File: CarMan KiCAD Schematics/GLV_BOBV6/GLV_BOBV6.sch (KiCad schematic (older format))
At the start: 31 parts, among them J1 Conn_01x02, J10 Conn_01x02, J11 Conn_01x02, J2 Conn_01x02, J3 Conn_01x02, J4 Conn_01x02, J5 Conn_01x02, J6 Conn_01x04, J7 Conn_01x02, J8 Conn_01x02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

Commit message: Added 24v to connection between GLV and Logic and updated headers accordingly
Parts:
- removed J5: Conn_01x02, symbol Connector_Generic:Conn_01x02
- removed J6: Conn_01x04, symbol Connector_Generic:Conn_01x04
- added J5, J8: Conn_02x02_Odd_Even, symbol Connector_Generic:Conn_02x02_Odd_Even
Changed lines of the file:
@@
 EESchema Schematic File Version 4
-EELAYER 30 0
+LIBS:GLV_BOBV6-cache
+EELAYER 29 0
 EELAYER END
 $Descr A4 11693 8268
@@
 Wire Wire Line
 	5400 3900 5400 4400
-Text Notes 5200 1500 0    50   ~ 10
+Text Notes 5450 1500 0    50   ~ 10
 Connection to Logic Board\nfor the I2C line. \n
 Text Notes 1800 1400 0    50   ~ 10
 From LSP/Ammeter
-Text Notes 2150 2750 0    50   ~ 10
+Text Notes 2200 2700 0    50   ~ 10
 24V to TSI/Analog\nBoard and SL. \nTSI calls SLOOP_TO_IMD Sl1_in
 Text Notes 3350 1450 0    50   ~ 10
@@
 Text Label 7700 1450 1    50   ~ 0
 BREAKER_OUT_GENERAL
-$Comp
-L Connector_Generic:Conn_01x04 J6
-U 1 1 5F9FEFCD
-P 2500 2400
-F 0 "J6" V 2418 2580 50  0000 C BNB
-F 1 "Conn_01x04" H 2580 2301 50  0001 L CNN
-F 2 "" H 2500 2400 50  0001 C CNN
-F 3 "~" H 2500 2400 50  0001 C CNN
-	1    2500 2400
-	0    1    1    0
-$EndComp
-Text Label 2500 2200 1    50   ~ 0
-GLV_RTN
-Text Label 2400 2200 1    50   ~ 0
-SLOOP_TO_IMD
-Text Label 2600 2200 1    50   ~ 0
-24V
 Text Label 5950 1950 2    50   ~ 0
 BATT+
@@
 Text Label 3950 2250 1    50   ~ 0
 GLV_RTN
-NoConn ~ 2300 2200
 Wire Notes Line
 	7300 550  7300 2950
@@
 	5850 6400 6200 6400
 Connection ~ 5850 6400
-$Comp
-L Connector_Generic:Conn_01x02 J5
-U 1 1 5FAD8972
-P 5650 1250
-F 0 "J5" V 5568 1330 50  0000 L CNB
-F 1 "Conn_01x02" V 5613 1330 50  0001 L CNN
-F 2 "" H 5650 1250 50  0001 C CNN
-F 3 "~" H 5650 1250 50  0001 C CNN
-	1    5650 1250
-	0    1    1    0
-$EndComp
 Text Label 1700 2050 3    50   ~ 10
 SLOOP_TO_IMD
@@
 	1    0    0    -1
 $EndComp
-Text Label 5550 1050 1    50   ~ 0
+$Comp
+L Connector_Generic:Conn_02x02_Odd_Even J5
+U 1 1 5FB21308
+P 5800 1100
+F 0 "J5" H 5850 1225 50  0000 C CNB
+F 1 "Conn_02x02_Odd_Even" H 5850 1226 50  0001 C CNN
+F 2 "" H 5800 1100 50  0001 C CNN
+F 3 "~" H 5800 1100 50  0001 C CNN
+	1    5800 1100
+	1    0    0    -1
+$EndComp
+$Comp
+L Connector_Generic:Conn_02x02_Odd_Even J8
+U 1 1 5FB2255E
+P 2700 2250
+F 0 "J8" H 2750 2375 50  0000 C CNB
+F 1 "Conn_02x02_Odd_Even" H 2750 2376 50  0001 C CNN
+F 2 "" H 2700 2250 50  0001 C CNN
+F 3 "~" H 2700 2250 50  0001 C CNN
+	1    2700 2250
+	1    0    0    -1
+$EndComp
+Text Label 5600 1100 2    50   ~ 0
 SCL_NOT_ISO
-Text Label 5650 1050 1    50   ~ 0
+Text Label 6100 1100 0    50   ~ 0
 SDA_NOT_ISO
+Text Label 5600 1200 2    50   ~ 0
+GLV_RTN
+Text Label 6100 1200 0    50   ~ 0
+24V
+NoConn ~ 3000 2350
+Text Label 2500 2250 2    50   ~ 0
+24V
+Text Label 3000 2250 0    50   ~ 0
+GLV_RTN
+Text Label 2500 2350 2    50   ~ 0
+SLOOP_TO_IMD
 $EndSCHEMATC

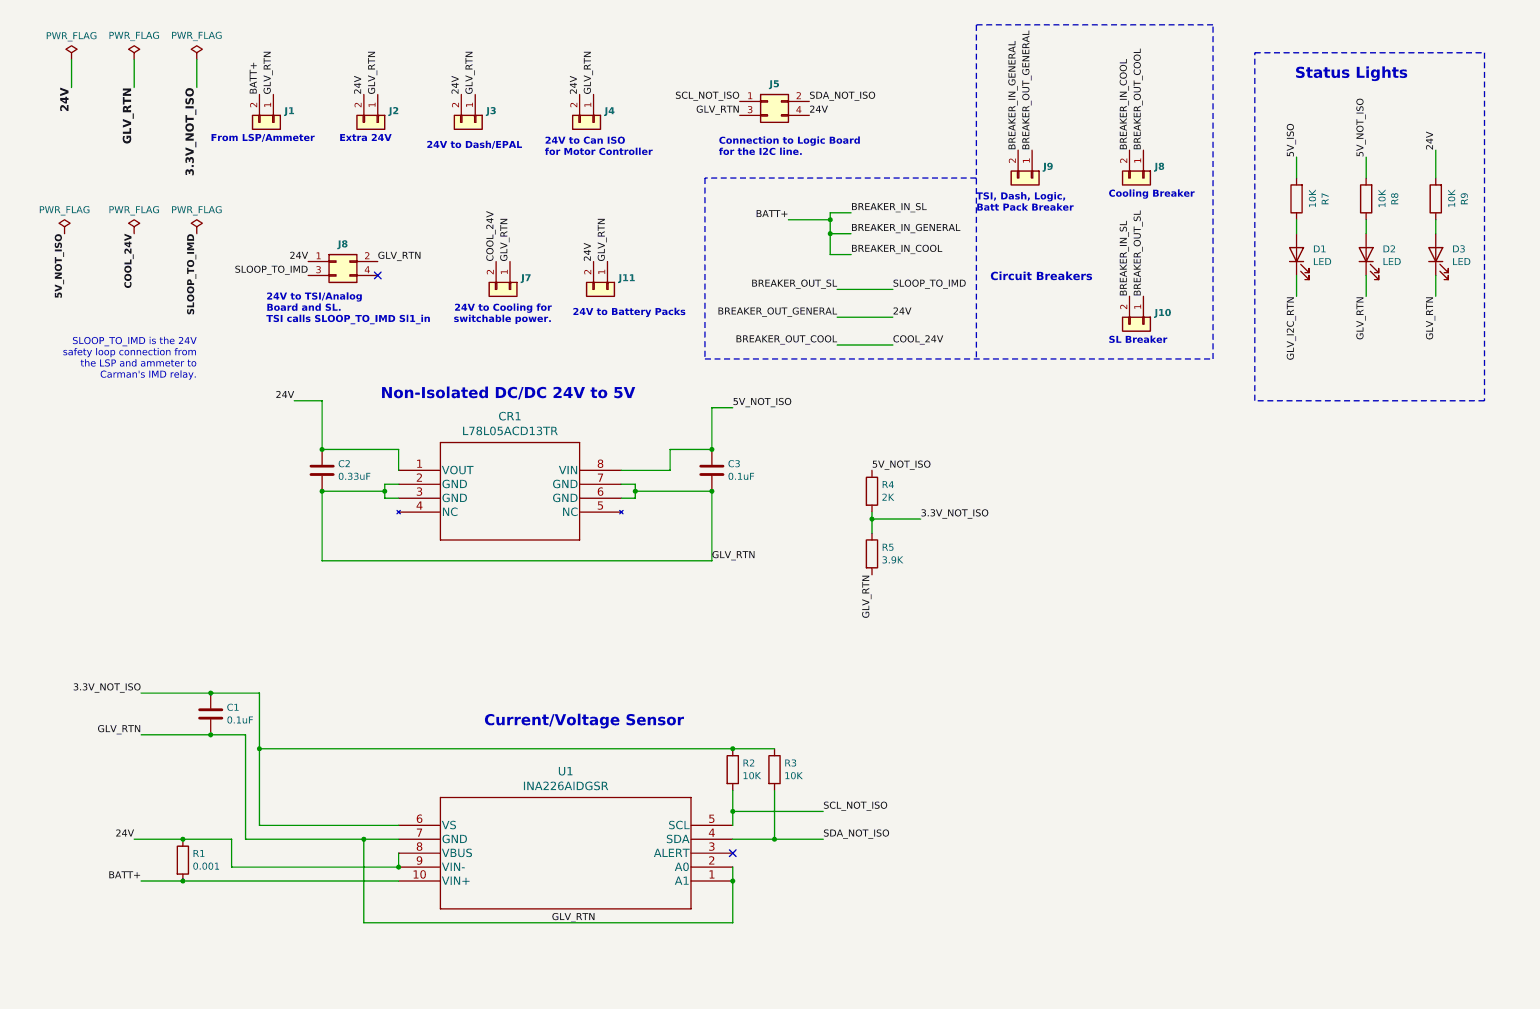
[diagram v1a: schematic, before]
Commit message: Carman Footprint Library, GLV PCB v1
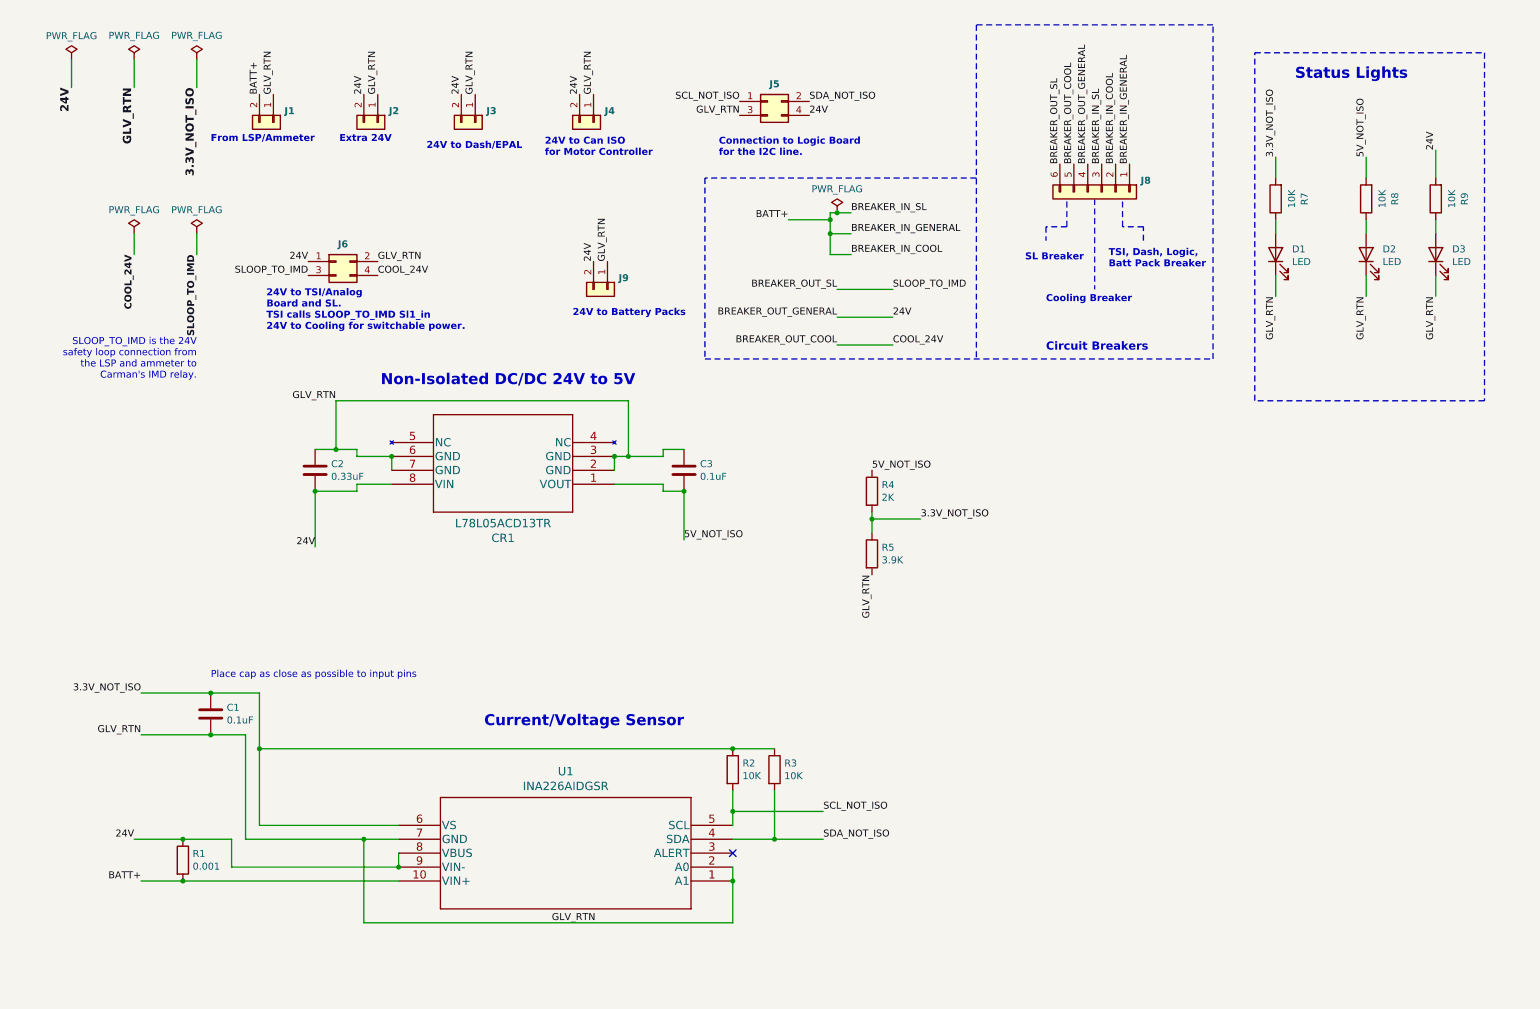
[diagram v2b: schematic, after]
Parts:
- removed 24V01, 24V02, 24V03, 24V04: PWR_FLAG, symbol power:PWR_FLAG
- removed J10, J7, J8, J9: Conn_01x02, symbol Connector_Generic:Conn_01x02
- added J8: J8, CarMan General Footprints:Molex_MiniFit-JR-5556-06A_2x03x4.20mm_Straight, symbol Connector_Generic:Conn_01x06
- C1, C2, C3: footprint (none) -> Capacitor_SMD:C_0805_2012Metric_Pad1.15x1.40mm_HandSolder
- CR1: footprint SO-8_STM -> CarMan General Footprints:L78L05ACD13TR
- D1, D2, D3: footprint (none) -> CarMan General Footprints:VAOL-S8GT4
- J1, J2, J3, J4: footprint (none) -> CarMan General Footprints:Molex_MiniFit-JR-5556-02A_2x01x4.20mm_Straight
- J5: footprint (none) -> CarMan General Footprints:Molex_MiniFit-JR-5556-04A_2x02x4.20mm_Straight
- J6: renamed from J8; footprint (none) -> CarMan General Footprints:Molex_MiniFit-JR-5556-04A_2x02x4.20mm_Straight
- J9: renamed from J11; footprint (none) -> CarMan General Footprints:Molex_MiniFit-JR-5556-02A_2x01x4.20mm_Straight
- R1: footprint (none) -> Resistor_SMD:R_1210_3225Metric_Pad1.42x2.65mm_HandSolder
- R2, R3, R4, R5, R7, R8, R9: footprint (none) -> Resistor_SMD:R_0805_2012Metric_Pad1.15x1.40mm_HandSolder
- U1: footprint DGS10 -> CarMan General Footprints:INA226AIDGSR
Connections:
- net 5V_ISO is gone; now on net 3.3V_NOT_ISO: R7.2
- net GLV_I2C_RTN is gone; now on net GLV_RTN: D1.1 (K)
- net 24V: now also C2.2, CR1.8 (VIN), J8.4 (Pin_4); no longer C2.1, CR1.1 (VOUT)
- net 5V_NOT_ISO: now also C3.2, CR1.1 (VOUT); no longer C3.1, CR1.8 (VIN)
- net BATT+: now also J8.1 (Pin_1), J8.2 (Pin_2), J8.3 (Pin_3)
- net BREAKER_OUT_COOL: now also J6.4 (Pin_4), J8.5 (Pin_5)
- net BREAKER_OUT_SL: now also J8.6 (Pin_6)
- net GLV_RTN: now also C2.1, C3.1; no longer C2.2, C3.2
- no-connect marks 2 -> 1
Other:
- note added: "24V to TSI/Analog\nBoard and SL. \nTSI calls SLOOP_TO_IMD Sl1_in\n24V to Cooling for switchable power."
- note added: "Place cap as close as possible to input pins"
- note removed: "24V to Cooling for\nswitchable power."
- note removed: "24V to TSI/Analog\nBoard and SL. \nTSI calls SLOOP_TO_IMD Sl1_in"
- moved on the sheet: C2, C3, CR1, D1, R7

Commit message: GLV PCB edge cuts, logos, increased BATT+ trace widths, Gerber files
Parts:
- added H1, H2, H3, H4: MountingHole, MountingHole:MountingHole_2.5mm_Pad, symbol Mechanical:MountingHole
- U1: symbol CarMan_KiCAD_Library:INA226AIDGSR -> GLV_BOBV6-rescue:INA226AIDGSR-CarMan_KiCAD_Library
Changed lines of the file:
@@
 Extra 24V
 $Comp
-L CarMan_KiCAD_Library:INA226AIDGSR U?
+L GLV_BOBV6-rescue:INA226AIDGSR-CarMan_KiCAD_Library U?
 U 1 1 5FABD1EB
 P 5550 6700
@@
 Text Notes 1800 5250 0    50   ~ 0
 Place cap as close as possible to input pins
+$Comp
+L Mechanical:MountingHole H1
+U 1 1 5FBABE36
+P 9000 3700
+F 0 "H1" H 9100 3746 50  0000 L CNN
+F 1 "MountingHole" H 9100 3655 50  0000 L CNN
+F 2 "MountingHole:MountingHole_2.5mm_Pad" H 9000 3700 50  0001 C CNN
+F 3 "~" H 9000 3700 50  0001 C CNN
+	1    9000 3700
+	1    0    0    -1
+$EndComp
+$Comp
+L Mechanical:MountingHole H4
+U 1 1 5FBADD6E
+P 10550 3700
+F 0 "H4" H 10650 3746 50  0000 L CNN
+F 1 "MountingHole" H 10650 3655 50  0000 L CNN
+F 2 "MountingHole:MountingHole_2.5mm_Pad" H 10550 3700 50  0001 C CNN
+F 3 "~" H 10550 3700 50  0001 C CNN
+	1    10550 3700
+	1    0    0    -1
+$EndComp
+$Comp
+L Mechanical:MountingHole H3
+U 1 1 5FBAE047
+P 10500 4800
+F 0 "H3" H 10600 4846 50  0000 L CNN
+F 1 "MountingHole" H 10600 4755 50  0000 L CNN
+F 2 "MountingHole:MountingHole_2.5mm_Pad" H 10500 4800 50  0001 C CNN
+F 3 "~" H 10500 4800 50  0001 C CNN
+	1    10500 4800
+	1    0    0    -1
+$EndComp
+$Comp
+L Mechanical:MountingHole H2
+U 1 1 5FBAE1E6
+P 9000 4750
+F 0 "H2" H 9100 4796 50  0000 L CNN
+F 1 "MountingHole" H 9100 4705 50  0000 L CNN
+F 2 "MountingHole:MountingHole_2.5mm_Pad" H 9000 4750 50  0001 C CNN
+F 3 "~" H 9000 4750 50  0001 C CNN
+	1    9000 4750
+	1    0    0    -1
+$EndComp
 $EndSCHEMATC

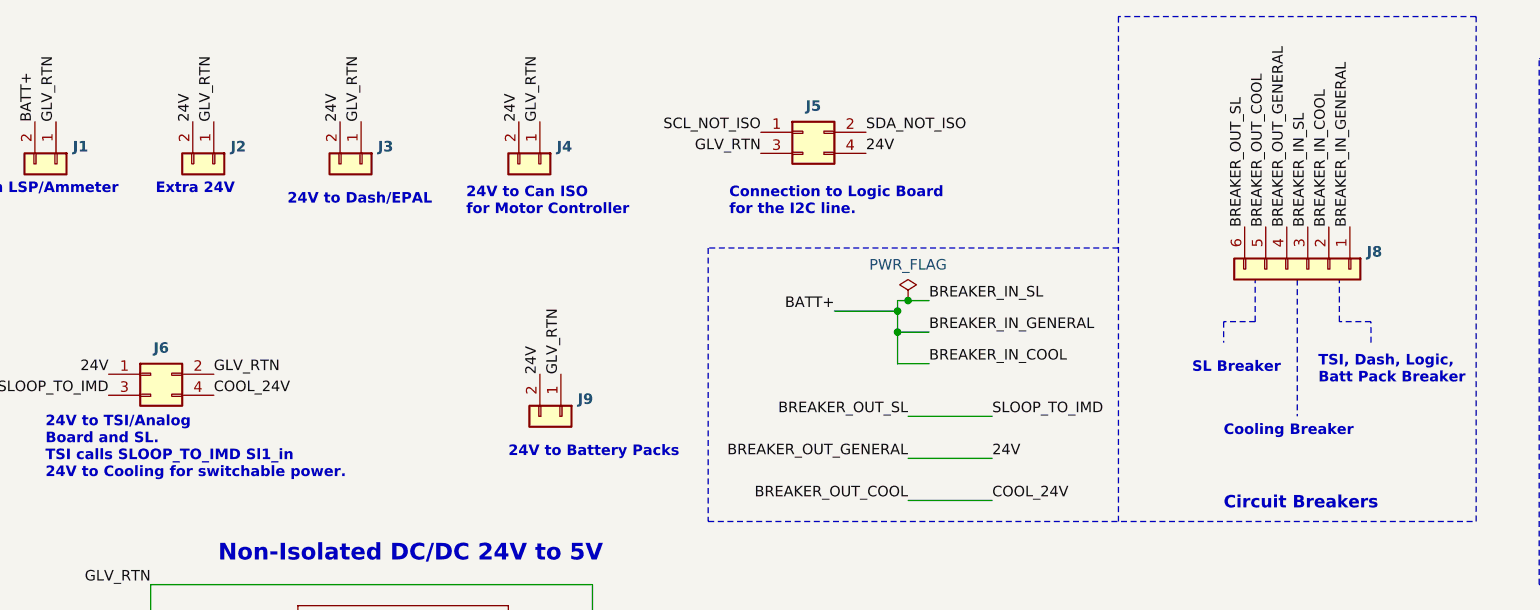
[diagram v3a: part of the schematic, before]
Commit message: GLV removed 24V to dash and 24V to BP headers. Logic almost done pending, design review
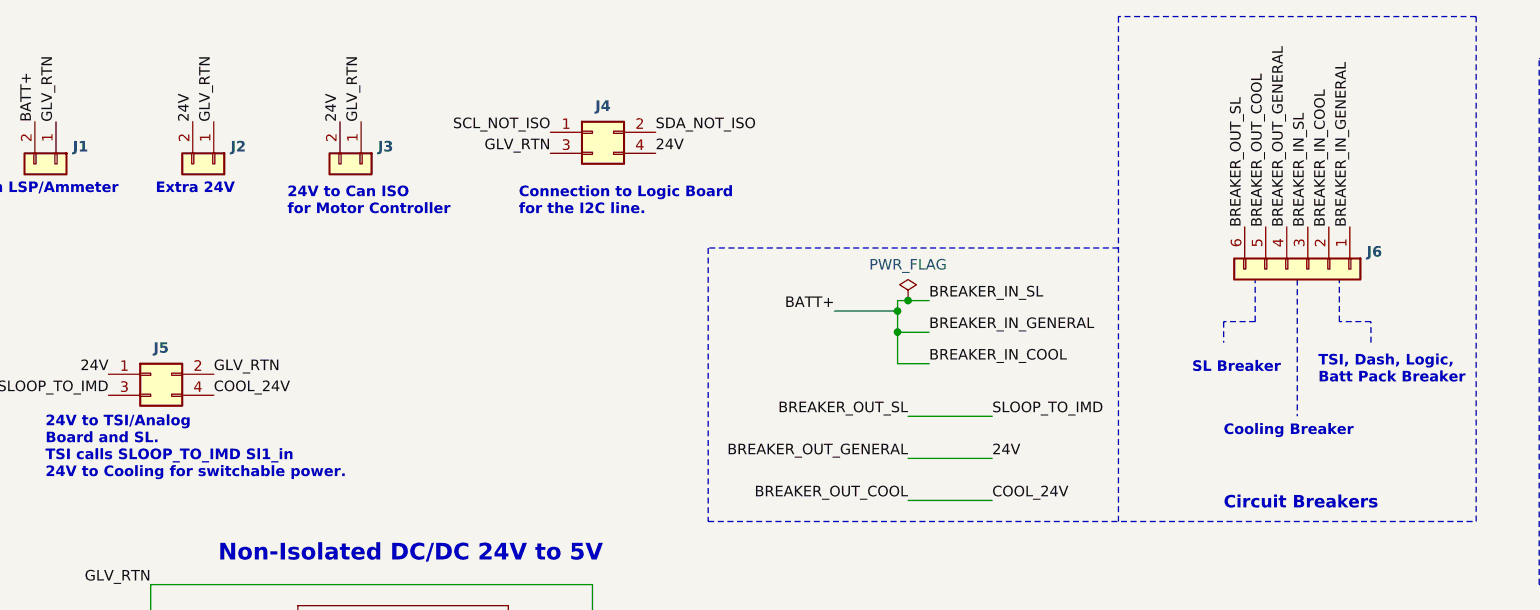
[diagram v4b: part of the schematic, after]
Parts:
- removed J4, J9: Conn_01x02, CarMan General Footprints:Molex_MiniFit-JR-5556-02A_2x01x4.20mm_Straight, symbol Connector_Generic:Conn_01x02
- J6: renamed from J8; value J8 -> J6
- renumbered J5 to J4, J6 to J5
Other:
- note removed: "24V to Battery Packs"
- note removed: "24V to Dash/EPAL"
- moved on the sheet: J4
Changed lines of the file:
@@
 Text Label 2550 4300 2    50   ~ 0
 24V
-Text Notes 5450 1500 0    50   ~ 10
+Text Notes 4450 1500 0    50   ~ 10
 Connection to Logic Board\nfor the I2C line. \n
 Text Notes 1800 1400 0    50   ~ 10
@@
 Text Notes 2200 2750 0    50   ~ 10
 24V to TSI/Analog\nBoard and SL. \nTSI calls SLOOP_TO_IMD Sl1_in\n24V to Cooling for switchable power.
-Text Notes 3350 1450 0    50   ~ 10
-24V to Dash/EPAL
-Text Notes 4200 1500 0    50   ~ 10
+Text Notes 3350 1500 0    50   ~ 10
 24V to Can ISO\nfor Motor Controller
 Text Notes 7650 2250 0    50   ~ 10
 SL Breaker\n
-Text Notes 4400 2650 0    50   ~ 10
-24V to Battery Packs
 $Comp
 L Device:LED D2
@@
 Text Label 3600 1050 1    50   ~ 0
 24V
-$Comp
-L Connector_Generic:Conn_01x02 J4
-U 1 1 5FA2FDEA
-P 4550 1250
-F 0 "J4" V 4468 1330 50  0000 L CNB
-F 1 "Conn_01x02" V 4513 1330 50  0001 L CNN
-F 2 "CarMan General Footprints:Molex_MiniFit-JR-5556-02A_2x01x4.20mm_Straight" H 4550 1250 50  0001 C CNN
-F 3 "~" H 4550 1250 50  0001 C CNN
-	1    4550 1250
-	0    1    1    0
-$EndComp
-Text Label 4450 1050 1    50   ~ 0
-24V
-Text Label 4550 1050 1    50   ~ 0
-GLV_RTN
-$Comp
-L Connector_Generic:Conn_01x02 J9
-U 1 1 5FA3AB0D
-P 4650 2450
-F 0 "J9" V 4568 2530 50  0000 L CNB
-F 1 "Conn_01x02" V 4613 2530 50  0001 L CNN
-F 2 "CarMan General Footprints:Molex_MiniFit-JR-5556-02A_2x01x4.20mm_Straight" H 4650 2450 50  0001 C CNN
-F 3 "~" H 4650 2450 50  0001 C CNN
-	1    4650 2450
-	0    1    1    0
-$EndComp
-Text Label 4550 2250 1    50   ~ 0
-24V
-Text Label 4650 2250 1    50   ~ 0
-GLV_RTN
 Text Label 3000 2350 0    50   ~ 0
 COOL_24V
@@
 $EndComp
 $Comp
+L Connector_Generic:Conn_02x02_Odd_Even J4
+U 1 1 5FB21308
+P 4800 1100
+F 0 "J4" H 4850 1225 50  0000 C CNB
+F 1 "Conn_02x02_Odd_Even" H 4850 1226 50  0001 C CNN
+F 2 "CarMan General Footprints:Molex_MiniFit-JR-5556-04A_2x02x4.20mm_Straight" H 4800 1100 50  0001 C CNN
+F 3 "~" H 4800 1100 50  0001 C CNN
+	1    4800 1100
+	1    0    0    -1
+$EndComp
+$Comp
 L Connector_Generic:Conn_02x02_Odd_Even J5
-U 1 1 5FB21308
-P 5800 1100
-F 0 "J5" H 5850 1225 50  0000 C CNB
-F 1 "Conn_02x02_Odd_Even" H 5850 1226 50  0001 C CNN
-F 2 "CarMan General Footprints:Molex_MiniFit-JR-5556-04A_2x02x4.20mm_Straight" H 5800 1100 50  0001 C CNN
-F 3 "~" H 5800 1100 50  0001 C CNN
-	1    5800 1100
-	1    0    0    -1
-$EndComp
-$Comp
-L Connector_Generic:Conn_02x02_Odd_Even J6
 U 1 1 5FB2255E
 P 2700 2250
-F 0 "J6" H 2750 2375 50  0000 C CNB
+F 0 "J5" H 2750 2375 50  0000 C CNB
 F 1 "Conn_02x02_Odd_Even" H 2750 2376 50  0001 C CNN
 F 2 "CarMan General Footprints:Molex_MiniFit-JR-5556-04A_2x02x4.20mm_Straight" H 2700 2250 50  0001 C CNN
@@
 	1    0    0    -1
 $EndComp
-Text Label 5600 1100 2    50   ~ 0
+Text Label 4600 1100 2    50   ~ 0
 SCL_NOT_ISO
-Text Label 6100 1100 0    50   ~ 0
+Text Label 5100 1100 0    50   ~ 0
 SDA_NOT_ISO
-Text Label 5600 1200 2    50   ~ 0
-GLV_RTN
-Text Label 6100 1200 0    50   ~ 0
+Text Label 4600 1200 2    50   ~ 0
+GLV_RTN
+Text Label 5100 1200 0    50   ~ 0
 24V
 Text Label 2500 2250 2    50   ~ 0
@@
 GLV_RTN
 $Comp
-L Connector_Generic:Conn_01x06 J8
+L Connector_Generic:Conn_01x06 J6
 U 1 1 5FBB1F11
 P 8200 1750
-F 0 "J8" V 8118 2030 50  0000 L CNB
-F 1 "J8" V 8163 2030 50  0001 L CNN
+F 0 "J6" V 8118 2030 50  0000 L CNB
+F 1 "J6" V 8163 2030 50  0001 L CNN
 F 2 "CarMan General Footprints:Molex_MiniFit-JR-5556-06A_2x03x4.20mm_Straight" H 8200 1750 50  0001 C CNN
 F 3 "~" H 8200 1750 50  0001 C CNN

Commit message: GLV DR Fixes
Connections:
- net 24V: no longer R1.1, U1.8 (VBUS), U1.9 (VIN-)
- net BATT+: no longer J6.1 (Pin_1), J6.2 (Pin_2), J6.3 (Pin_3)
- new net 24V_NOT_BREAKERED: J6.1 (Pin_1), J6.2 (Pin_2), J6.3 (Pin_3), R1.1, U1.8 (VBUS), U1.9 (VIN-)
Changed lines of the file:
@@
 Text Notes 8250 2300 0    50   ~ 10
 TSI, Dash, Logic,\nBatt Pack Breaker
-Text Label 5950 1950 2    50   ~ 0
-BATT+
 Wire Wire Line
 	5950 1950 6250 1950
@@
 GLV_RTN
 Text Label 1250 6400 2    50   ~ 0
-24V
+24V_NOT_BREAKERED
 Text Label 1300 6700 2    50   ~ 0
 BATT+
@@
 	1    0    0    -1
 $EndComp
+Text Label 5950 1950 2    50   ~ 0
+24V_NOT_BREAKERED
 $EndSCHEMATC
